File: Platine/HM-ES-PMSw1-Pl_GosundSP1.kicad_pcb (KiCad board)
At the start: 2 copper layers, 23.2 x 20.7 mm, 13 parts, among them J11 BW_Gosund_Con, J4 Reset, U1 ATMEGA644PA-AU, U2 CC1101, Y1 Resonator

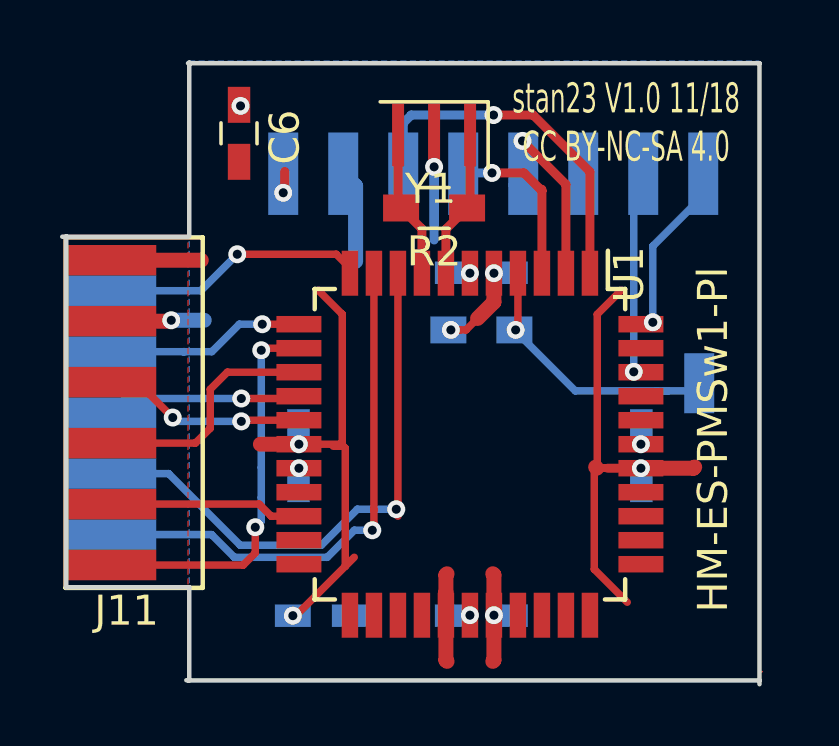
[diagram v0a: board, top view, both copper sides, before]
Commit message: fix wrong blue LED and button for Gosund SP1 V2.3
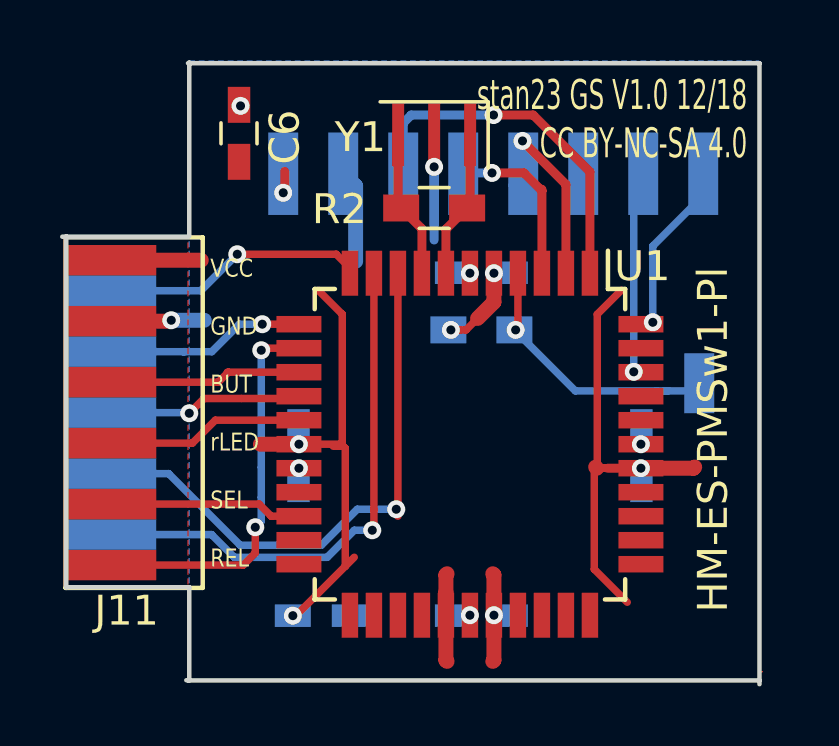
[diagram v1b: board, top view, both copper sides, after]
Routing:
- net /BUTTON: track 8.00 -> 6.42 mm
- net /LED_red: track 6.99 -> 6.57 mm, vias 2 -> 0
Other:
- board text added: "CF1 CF bLED RX TX"
- board text added: "VCC GND BUT rLED SEL REL"
- board text added: "stan23 GS V1.0 12/18 CC BY-NC-SA 4.0"
- board text removed: "stan23 V1.0 11/18 CC BY-NC-SA 4.0"
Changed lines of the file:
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@@
     (area 86.511081 90.39468 128.75408 119.921081)
     (thickness 1.6)
-    (drawings 17)
-    (tracks 218)
+    (drawings 19)
+    (tracks 210)
     (zones 0)
     (modules 13)
@@
     (tags "QFP 0.8")
     (attr smd)
-    (fp_text reference U1 (at -5.656854 -5.303301 270) (layer F.SilkS)
+    (fp_text reference U1 (at -5.932 -5.745 360) (layer F.SilkS)
       (effects (font (size 1 1) (thickness 0.15)))
     )
@@
     (tags "resistor 0603")
     (attr smd)
-    (fp_text reference R2 (at 0 -1.45 180) (layer F.SilkS)
+    (fp_text reference R2 (at 3.1612 -0.042 180) (layer F.SilkS)
       (effects (font (size 1 1) (thickness 0.15)))
     )
@@
     (tags "SMD SMT ceramic resonator filter filter hand-soldering")
     (attr smd)
-    (fp_text reference Y1 (at 0.12 -1.8 180) (layer F.SilkS)
+    (fp_text reference Y1 (at 2.4612 -0.0804 180) (layer F.SilkS)
       (effects (font (size 1 1) (thickness 0.15)))
     )
@@
   (module Testpads:Testpad (layer B.Cu)
     (at 117.50048 101.60008)
-    (fp_text reference J4 (at 0.0762 3.1496 90) (layer B.SilkS)
+    (fp_text reference J4 (at 0.4996 2 90) (layer B.SilkS)
       (effects (font (size 1 1) (thickness 0.15)) (justify mirror))
     )
@@
     (pad REL smd rect (at 10.16 0) (size 3 1.016) (layers F.Cu F.Paste F.Mask)
       (net 29 /RELAY))
-    (pad BUT smd rect (at 6.096 0) (size 3 1.016) (layers F.Cu F.Paste F.Mask)
-      (net 30 /BUTTON))
+    (pad rLED smd rect (at 6.096 0) (size 3 1.016) (layers F.Cu F.Paste F.Mask)
+      (net 32 /LED_red))
     (pad bLED smd rect (at 5.08 0) (size 3 1.016) (layers B.Cu B.Paste B.Mask)
       (net 31 /LED_blue))
-    (pad rLED smd rect (at 4.064 0) (size 3 1.016) (layers F.Cu F.Paste F.Mask)
-      (net 32 /LED_red))
+    (pad BUT smd rect (at 4.064 0) (size 3 1.016) (layers F.Cu F.Paste F.Mask)
+      (net 30 /BUTTON))
     (pad CF smd rect (at 3.048 0) (size 3 1.016) (layers B.Cu B.Paste B.Mask)
       (net 33 /CF))
@@
       (net 2 VCC))
   )
+  (gr_text "CF1\n\nCF\n\nbLED\n\nRX\n\nTX" (at 101.90008 102.50008) (layer B.SilkS)
+    (effects (font (size 0.6 0.5) (thickness 0.125)) (justify left mirror))
+  )
+  (gr_text "VCC\n\nGND\n\nBUT\n\nrLED\n\nSEL\n\nREL" (at 101.20008 102.60008) (layer F.SilkS)
+    (effects (font (size 0.6 0.5) (thickness 0.125)) (justify left))
+  )
   (gr_line (start 100.50008 111.50008) (end 100.40008 111.50008) (angle 90) (layer Edge.Cuts) (width 0.15))
   (gr_line (start 100.50008 108.40008) (end 100.50008 111.50008) (angle 90) (layer Edge.Cuts) (width 0.15))
@@
   (gr_line (start 119.50708 90.93208) (end 100.45708 90.93208) (angle 90) (layer Edge.Cuts) (width 0.15))
   (gr_line (start 119.50708 111.50608) (end 119.50708 90.93208) (angle 90) (layer Edge.Cuts) (width 0.15))
-  (gr_text "stan23 V1.0 11/18\nCC BY-NC-SA 4.0" (at 115.06208 92.91328) (layer F.SilkS)
-    (effects (font (size 1 0.6) (thickness 0.125)))
+  (gr_text "stan23 GS V1.0 12/18\nCC BY-NC-SA 4.0" (at 119.10008 92.80008) (layer F.SilkS)
+    (effects (font (size 1 0.6) (thickness 0.125)) (justify right))
   )
   (segment (start 101.00008 99.50008) (end 99.90008 99.50008) (width 0.5) (layer B.Cu) (net 1))
@@
   (segment (start 109.85508 97.93208) (end 109.84008 97.91708) (width 0.25) (layer B.Cu) (net 1))
   (segment (start 109.84008 97.91708) (end 109.28608 97.91708) (width 0.25) (layer B.Cu) (net 1))
-  (segment (start 104.15508 103.63208) (end 105.56808 103.63208) (width 0.25) (layer F.Cu) (net 2) (status 400000))
+  (segment (start 97.90008 97.50008) (end 100.90008 97.50008) (width 0.5) (layer F.Cu) (net 2))
+  (segment (start 104.15508 103.63208) (end 105.56808 103.63208) (width 0.25) (layer F.Cu) (net 2))
   (segment (start 105.70008 103.76408) (end 105.70008 107.70008) (width 0.25) (layer F.Cu) (net 2))
   (segment (start 105.56808 103.63208) (end 105.70008 103.76408) (width 0.25) (layer F.Cu) (net 2))
@@
   (segment (start 114.10008 104.43208) (end 114.10008 99.30008) (width 0.25) (layer F.Cu) (net 2))
   (segment (start 114.10008 99.30008) (end 114.90008 98.50008) (width 0.25) (layer F.Cu) (net 2))
-  (segment (start 115.55508 104.43208) (end 114.10008 104.43208) (width 0.25) (layer F.Cu) (net 2) (status 400000))
+  (segment (start 115.55508 104.43208) (end 114.10008 104.43208) (width 0.25) (layer F.Cu) (net 2))
   (segment (start 114.10008 104.43208) (end 114.08408 104.43208) (width 0.25) (layer F.Cu) (net 2))
   (segment (start 114.08408 104.43208) (end 114.00008 104.51608) (width 0.25) (layer F.Cu) (net 2))
@@
   (segment (start 115.55508 104.43208) (end 114.16808 104.43208) (width 0.25) (layer F.Cu) (net 2))
   (segment (start 109.22008 99.82208) (end 109.52208 99.82208) (width 0.25) (layer F.Cu) (net 2))
-  (segment (start 97.90008 97.50008) (end 100.90008 97.50008) (width 0.5) (layer F.Cu) (net 2))
   (segment (start 115.55508 104.43208) (end 114.43968 104.43208) (width 0.3) (layer F.Cu) (net 2))
   (segment (start 103.68288 94.53888) (end 103.68288 95.19928) (width 0.3) (layer F.Cu) (net 2))
@@
   (segment (start 106.65508 105.81608) (end 106.65508 97.93208) (width 0.25) (layer F.Cu) (net 7))
   (segment (start 106.65508 105.81608) (end 106.65508 106.50008) (width 0.25) (layer F.Cu) (net 7))
-  (segment (start 98.06308 106.80708) (end 97.90008 106.64408) (width 0.25) (layer B.Cu) (net 7))
   (segment (start 107.45508 97.93208) (end 107.45508 106.03208) (width 0.25) (layer F.Cu) (net 8))
   (segment (start 97.90008 104.61208) (end 99.81208 104.61208) (width 0.25) (layer B.Cu) (net 8))
@@
   (segment (start 102.90008 106.20008) (end 102.70008 106.40008) (width 0.25) (layer B.Cu) (net 29))
   (segment (start 97.90008 107.66008) (end 102.30008 107.66008) (width 0.25) (layer F.Cu) (net 29))
-  (segment (start 98.14568 107.69608) (end 97.84088 107.39128) (width 0.25) (layer F.Cu) (net 29) (status 30))
   (segment (start 104.15508 100.43208) (end 104.13008 100.45708) (width 0.25) (layer F.Cu) (net 29))
-  (segment (start 104.15508 101.23208) (end 101.76808 101.23208) (width 0.25) (layer F.Cu) (net 30))
-  (segment (start 100.70408 103.59608) (end 97.90008 103.59608) (width 0.25) (layer F.Cu) (net 30))
-  (segment (start 101.20008 103.10008) (end 100.70408 103.59608) (width 0.25) (layer F.Cu) (net 30))
-  (segment (start 101.20008 101.80008) (end 101.20008 103.10008) (width 0.25) (layer F.Cu) (net 30))
-  (segment (start 101.76808 101.23208) (end 101.20008 101.80008) (width 0.25) (layer F.Cu) (net 30))
-  (segment (start 98.37208 102.10808) (end 102.23508 102.10808) (width 0.25) (layer B.Cu) (net 31))
-  (via (at 102.23508 102.10808) (size 0.6) (drill 0.3) (layers F.Cu B.Cu) (net 31))
-  (segment (start 102.23508 102.10808) (end 104.07908 102.10808) (width 0.25) (layer F.Cu) (net 31))
-  (segment (start 98.37208 102.10808) (end 97.90008 102.58008) (width 0.25) (layer B.Cu) (net 31))
+  (segment (start 101.80008 101.23208) (end 101.46808 101.56408) (width 0.25) (layer F.Cu) (net 30))
+  (segment (start 101.46808 101.56408) (end 97.90008 101.56408) (width 0.25) (layer F.Cu) (net 30) (status 800000))
+  (segment (start 104.15508 101.23208) (end 101.80008 101.23208) (width 0.25) (layer F.Cu) (net 30))
+  (segment (start 101.80008 101.23208) (end 101.76808 101.23208) (width 0.25) (layer F.Cu) (net 30))
+  (segment (start 102.23508 102.10808) (end 100.99208 102.10808) (width 0.25) (layer F.Cu) (net 31))
+  (segment (start 104.07908 102.10808) (end 102.23508 102.10808) (width 0.25) (layer F.Cu) (net 31))
+  (segment (start 100.48008 102.58008) (end 97.90008 102.58008) (width 0.25) (layer B.Cu) (net 31) (status 800000))
+  (segment (start 100.50008 102.60008) (end 100.48008 102.58008) (width 0.25) (layer B.Cu) (net 31))
+  (via (at 100.50008 102.60008) (size 0.6) (drill 0.3) (layers F.Cu B.Cu) (net 31))
+  (segment (start 100.99208 102.10808) (end 100.50008 102.60008) (width 0.25) (layer F.Cu) (net 31))
   (segment (start 104.15508 102.03208) (end 104.07908 102.10808) (width 0.25) (layer F.Cu) (net 31))
-  (segment (start 98.77008 101.56408) (end 99.94908 102.74308) (width 0.25) (layer F.Cu) (net 32))
-  (segment (start 100.07608 102.87008) (end 102.23508 102.87008) (width 0.25) (layer B.Cu) (net 32))
-  (via (at 99.94908 102.74308) (size 0.6) (drill 0.3) (layers F.Cu B.Cu) (net 32))
-  (segment (start 99.94908 102.74308) (end 100.07608 102.87008) (width 0.25) (layer B.Cu) (net 32))
-  (segment (start 98.77008 101.56408) (end 97.90008 101.56408) (width 0.25) (layer F.Cu) (net 32))
-  (segment (start 102.40008 102.83208) (end 102.36208 102.87008) (width 0.25) (layer F.Cu) (net 32))
-  (segment (start 102.36208 102.87008) (end 102.23508 102.87008) (width 0.25) (layer F.Cu) (net 32))
-  (via (at 102.23508 102.87008) (size 0.6) (drill 0.3) (layers F.Cu B.Cu) (net 32))
-  (segment (start 104.15508 102.83208) (end 102.40008 102.83208) (width 0.25) (layer F.Cu) (net 32))
-  (segment (start 102.23508 102.87008) (end 102.10808 102.74308) (width 0.25) (layer B.Cu) (net 32))
+  (segment (start 104.15508 102.83208) (end 101.36808 102.83208) (width 0.25) (layer F.Cu) (net 32) (status 400000))
+  (segment (start 100.60408 103.59608) (end 97.90008 103.59608) (width 0.25) (layer F.Cu) (net 32) (status 800000))
+  (segment (start 101.36808 102.83208) (end 100.60408 103.59608) (width 0.25) (layer F.Cu) (net 32))
   (segment (start 100.30008 100.54808) (end 101.25208 100.54808) (width 0.25) (layer B.Cu) (net 33))
   (via (at 102.93308 99.63208) (size 0.6) (drill 0.3) (layers F.Cu B.Cu) (net 33))
